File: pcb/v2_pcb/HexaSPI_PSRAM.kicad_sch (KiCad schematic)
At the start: 5 parts, among them U3 APS512XXN-OB9-BG

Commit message: add rpls for 1v8, 5v
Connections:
- net GND: now also U3.E5 (VSS)
- net VSS renamed HEXASPI_IO7
- net HEXASPI_IO7: no longer U3.E5 (VSS)
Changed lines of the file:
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@@
+		)
+	)
+	(wire
+		(pts
+			(xy 173.99 93.98) (xy 173.99 96.52)
+		)
+		(stroke
+			(width 0)
+			(type default)
 		)
 	)
@@
 			)
 		)
-		(property "Value" "VDD_HEXASPI_M"
+		(property "Value" "+1V8_RUN"
 			(at 214.63 80.01 0)
 			(show_name no)

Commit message: pcb done
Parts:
- removed U3: APS512XXN-OB9-BG, APS512XXN-OB9-BG:BGA24C100P5X5_800X600X120, symbol noob:APS256XXN-OBR-BG
- added R302: 10k, Resistor_SMD:R_0402_1005Metric, symbol Device:R_Small_US
- added U3: APS512XXN-OB9-BG, open-race-v2:WLCSP-24_6x8mm_P1.0mm_APS512XXN, symbol open-race-v2:APS512XXN-OB9-BG
- C141: value 4.7uF -> 100nF; footprint (none) -> Capacitor_SMD:C_0402_1005Metric
- C142: footprint (none) -> Capacitor_SMD:C_0402_1005Metric
- C143: value 4.7uF -> 1uF; footprint (none) -> Capacitor_SMD:C_0603_1608Metric
- C144: value 100nF -> 4.7uF; footprint (none) -> Capacitor_SMD:C_0603_1608Metric
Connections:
- net GND: now also U3.C1 (VSS), U3.E5 (VSS)
- net VDD renamed +1V8_RUN
- net +1V8_RUN: now also R302.1, U3.D1 (VDD), U3.E4 (VDD)
- new net PSRAM_CLK: U3.B2 (CLK)
- new net PSRAM_DQS0: U3.C3 (DQS0/DM0)
- new net PSRAM_DQS1: U3.B3 (DQS1/DM1)
- new net PSRAM_IO0: U3.D3 (ADQ0)
- new net PSRAM_IO1: U3.D2 (ADQ1)
- new net PSRAM_IO10: U3.A2 (DQ10)
- new net PSRAM_IO11: U3.A4 (DQ11)
- new net PSRAM_IO12: U3.A5 (DQ12)
- new net PSRAM_IO13: U3.B4 (DQ13)
- new net PSRAM_IO14: U3.B5 (DQ14)
- new net PSRAM_IO15: U3.C5 (DQ15)
- new net PSRAM_IO2: U3.C4 (ADQ2)
- new net PSRAM_IO3: U3.D4 (ADQ3)
- new net PSRAM_IO4: U3.D5 (ADQ4)
- new net PSRAM_IO5: U3.E3 (ADQ5)
- new net PSRAM_IO6: U3.E2 (ADQ6)
- new net PSRAM_IO7: U3.E1 (ADQ7)
- new net PSRAM_IO8: U3.C2 (DQ8)
- new net PSRAM_IO9: U3.B1 (DQ9)
- new net PSRAM_NCS: R302.2, U3.A3 (CE#)
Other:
- note removed: "100 nF/4.7µF decoupling for each pair C1/D1"

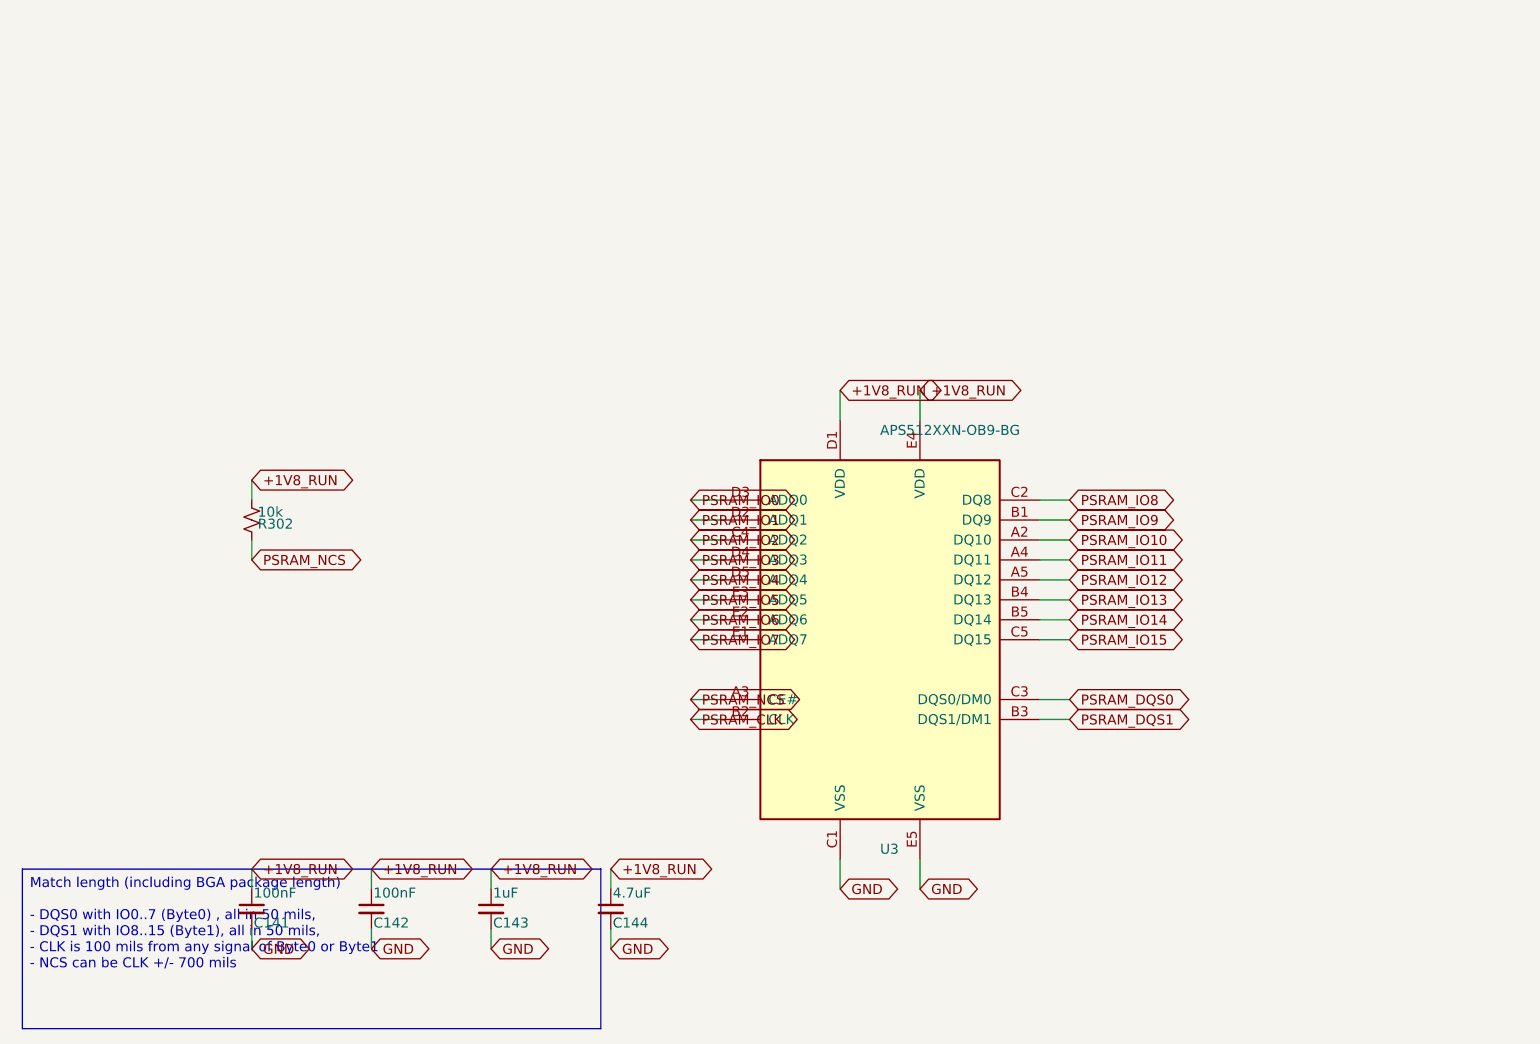
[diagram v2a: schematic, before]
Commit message: switch mosfets
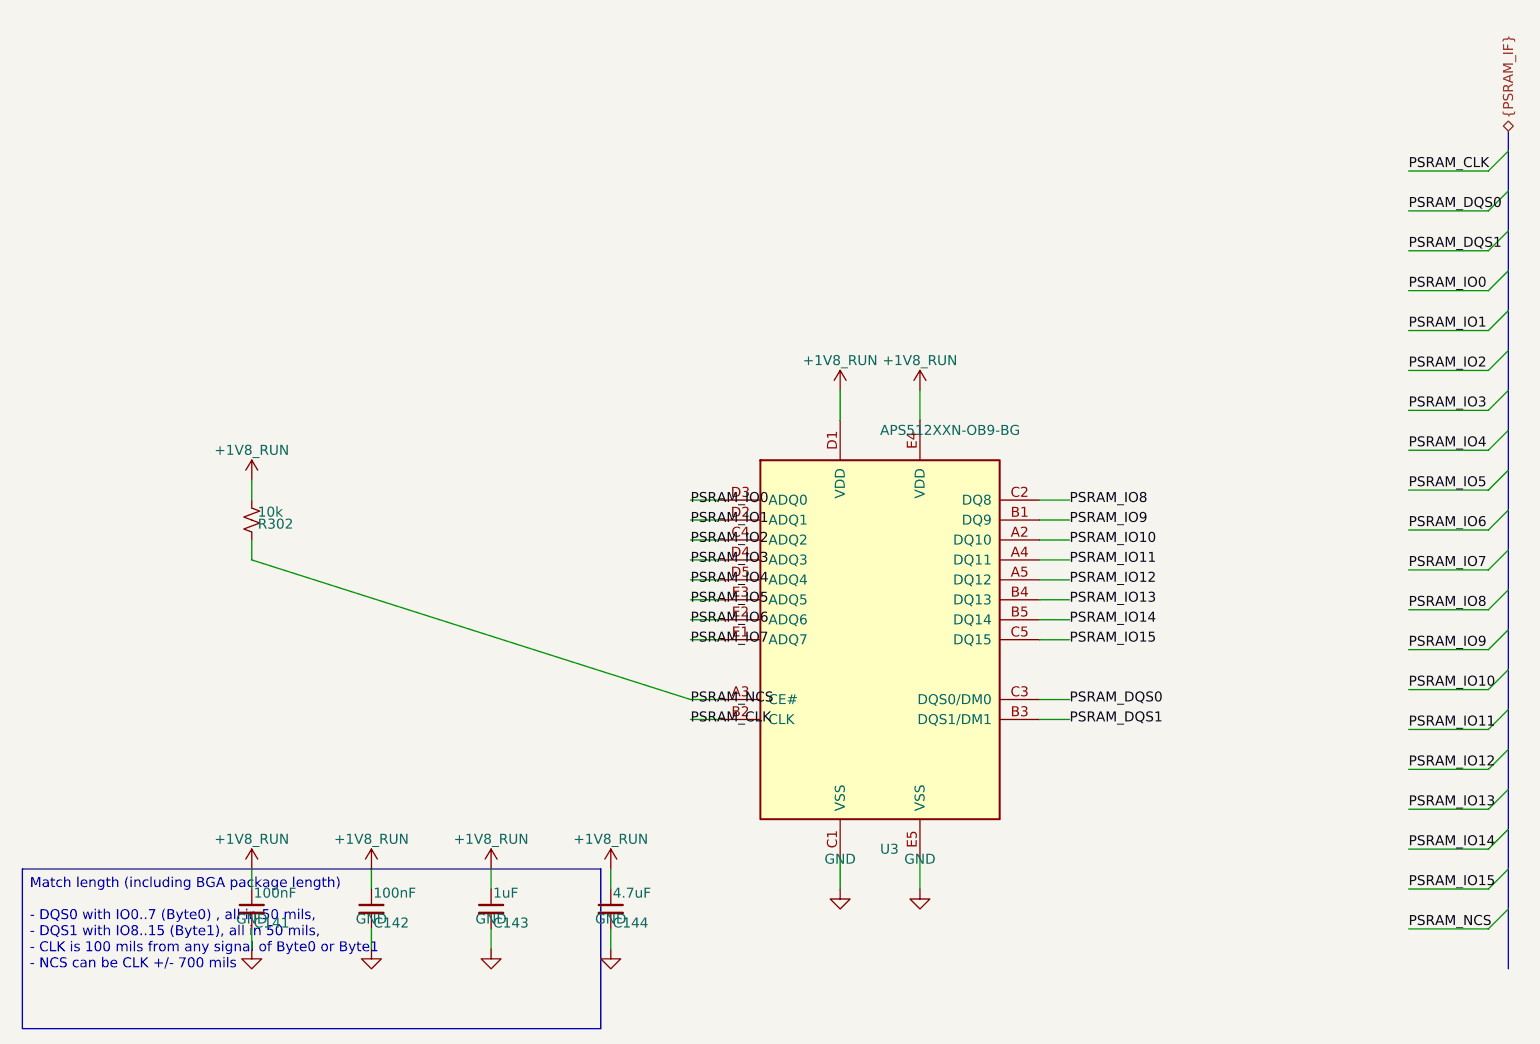
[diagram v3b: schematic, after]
